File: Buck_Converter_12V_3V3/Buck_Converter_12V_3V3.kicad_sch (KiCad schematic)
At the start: 0 parts

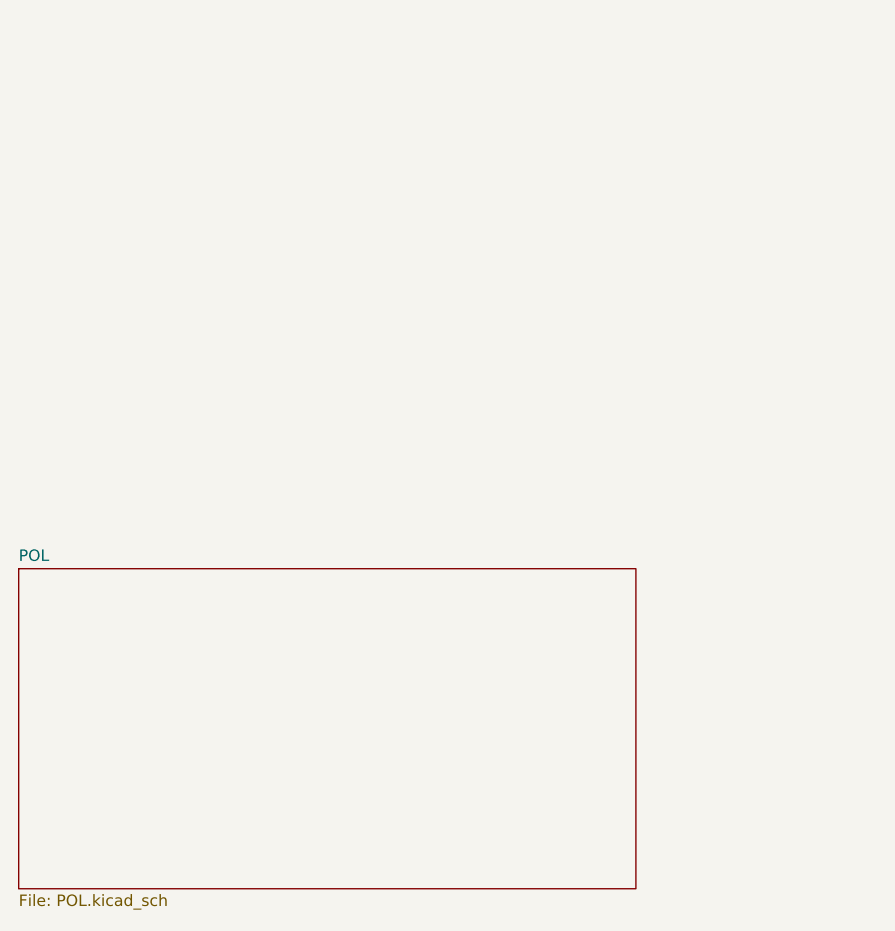
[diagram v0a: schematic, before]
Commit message: :construction: POL IC and input cpacitors added.
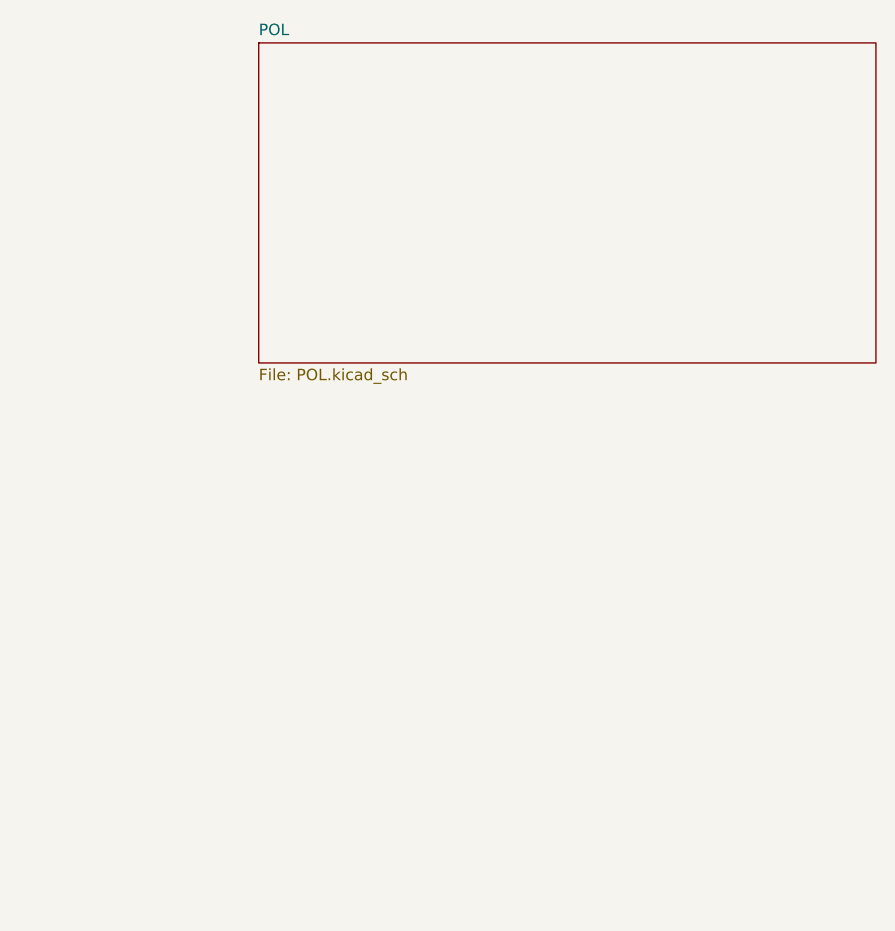
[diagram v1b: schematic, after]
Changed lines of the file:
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@@
 	(paper "A4")
 	(sheet
-		(at 38.1 132.08)
+		(at 64.77 73.66)
 		(size 68.58 35.56)
 		(fields_autoplaced yes)
@@
 		)
 		(property "Sheetname" "POL"
-			(at 38.1 131.3684 0)
+			(at 64.77 72.9484 0)
 			(effects
 				(font
@@
 		)
 		(property "Sheetfile" "POL.kicad_sch"
-			(at 38.1 168.2246 0)
+			(at 64.77 109.8046 0)
 			(effects
 				(font

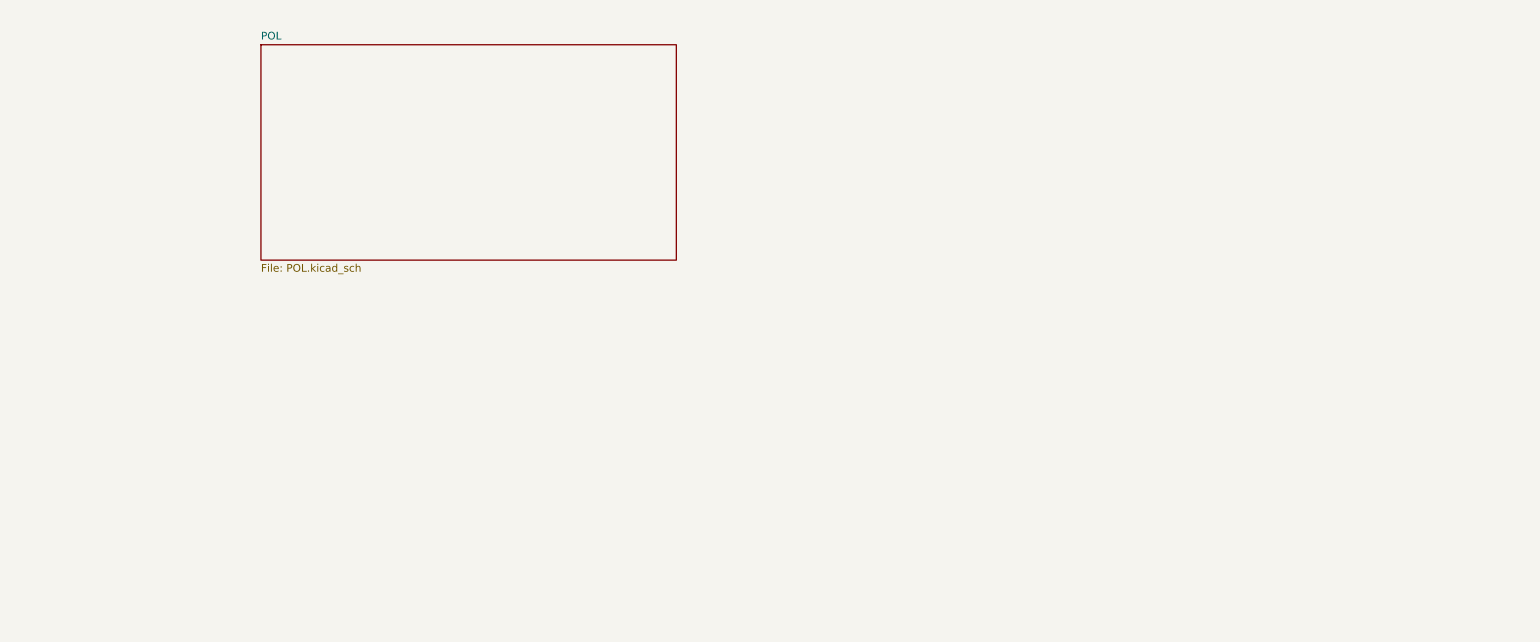
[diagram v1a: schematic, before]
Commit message: Layout Complete
Vis Stiching pending.
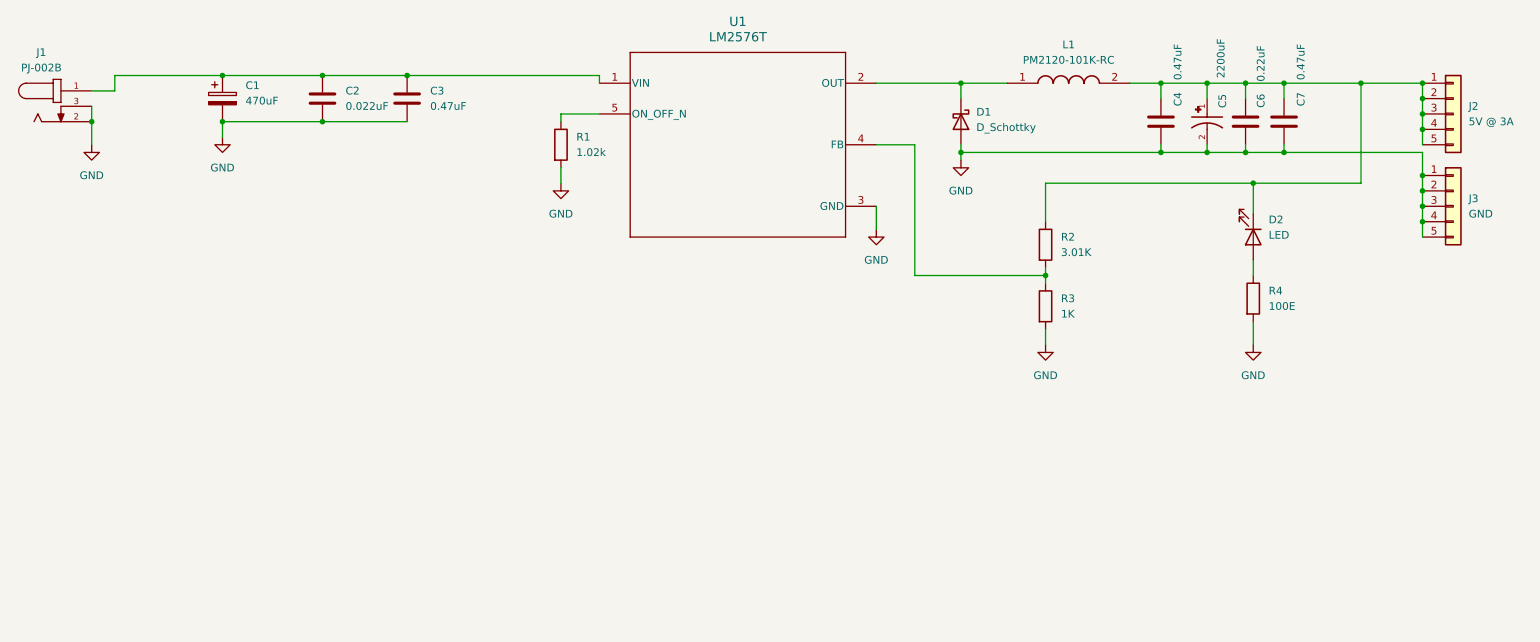
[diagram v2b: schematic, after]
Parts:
- added C1: 470uF, Capacitor:CAP_EEVFK1J471M, symbol Device:C_Polarized
- added C2: 0.022uF, Capacitor_SMD:C_0603_1608Metric_Pad1.08x0.95mm_HandSolder, symbol Device:C
- added C3, C4, C7: 0.47uF, Capacitor_SMD:C_1206_3216Metric_Pad1.33x1.80mm_HandSolder, symbol Device:C
- added C5: 2200uF, Capacitor:CAP_EEVFK1E222M, symbol Capacitor_1:EEVFK1E222M
- added C6: 0.22uF, Resistor_SMD:R_0603_1608Metric_Pad0.98x0.95mm_HandSolder, symbol Device:C
- added D1: D_Schottky, Diodes:SMC_DIO-M, symbol Device:D_Schottky
- added D2: LED, LED_THT:LED_D5.0mm, symbol Device:LED
- added J1: PJ-002B, Connector:CUI_PJ-002B, symbol Connector:PJ-002B
- added J2: 5V @ 3A, Connector_PinHeader_2.54mm:PinHeader_1x05_P2.54mm_Vertical, symbol Connector_Generic:Conn_01x05
- added J3: GND, Connector_PinHeader_2.54mm:PinHeader_1x05_P2.54mm_Vertical, symbol Connector_Generic:Conn_01x05
- added L1: PM2120-101K-RC, Inductor:PM2120271KRC, symbol Inductor:PM2120-101K-RC
- added R1: 1.02k, Resistor_SMD:R_1206_3216Metric_Pad1.30x1.75mm_HandSolder, symbol Device:R
- added R2: 3.01K, Resistor_SMD:R_1206_3216Metric_Pad1.30x1.75mm_HandSolder, symbol Device:R
- added R3: 1K, Resistor_SMD:R_1206_3216Metric_Pad1.30x1.75mm_HandSolder, symbol Device:R
- added R4: 100E, Resistor_SMD:R_1206_3216Metric_Pad1.30x1.75mm_HandSolder, symbol Device:R
- added U1: LM2576T, LM2576:LM2576xx, symbol LM2576:LM2576T-ADJ_NOPB
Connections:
- new net: D2.2 (A), R4.1
- new net: C4.1, C5.1, C6.1, C7.1, D2.1 (K), J2.1 (Pin_1), J2.2 (Pin_2), J2.3 (Pin_3), J2.4 (Pin_4), J2.5 (Pin_5), L1.2, R2.1
- new net: R1.1, U1.5 (ON_OFF_N)
- new net: C1.1, C2.1, C3.1, J1.1, U1.1 (VIN)
- new net: R2.2, R3.1, U1.4 (FB)
- new net: D1.1 (K), L1.1, U1.2 (OUT)
- new net GND: C1.2, C2.2, C3.2, C4.2, C5.2, C6.2, C7.2, D1.2 (A), J1.2, J1.3, J3.1 (Pin_1), J3.2 (Pin_2), J3.3 (Pin_3), J3.4 (Pin_4), J3.5 (Pin_5), R1.2, R3.2, R4.2, U1.3 (GND)
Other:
- removed sheet POL

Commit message: :rocket: Magicpower V1.0.0 Release
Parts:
- removed D2: LED, LED_THT:LED_D5.0mm, symbol Device:LED
- removed R2: 3.01K, Resistor_SMD:R_1206_3216Metric_Pad1.30x1.75mm_HandSolder, symbol Device:R
- removed R3: 1K, Resistor_SMD:R_1206_3216Metric_Pad1.30x1.75mm_HandSolder, symbol Device:R
- removed R4: 100E, Resistor_SMD:R_1206_3216Metric_Pad1.30x1.75mm_HandSolder, symbol Device:R
- added RV1: R_Potentiometer, SS_Resistors:601030_AVX, symbol Device:R_Potentiometer
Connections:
- net GND: now also RV1.3
- net at C4.1, C5.1, C6.1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: now also RV1.1
- net at U1.4 (FB): now also RV1.2
